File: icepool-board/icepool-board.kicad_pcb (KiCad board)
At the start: 4 copper layers, 90 x 40 mm, 101 parts, among them J1 PWR, J2 PWR_IN, J3 I2C, J4 SWD, J5 8P8C_Shielded, J6 8P8C_Shielded, SW1 B3U-1000P, U1 LD1117S33CTR, U2 LD1117S12CTR, U3 ATSAMD21E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

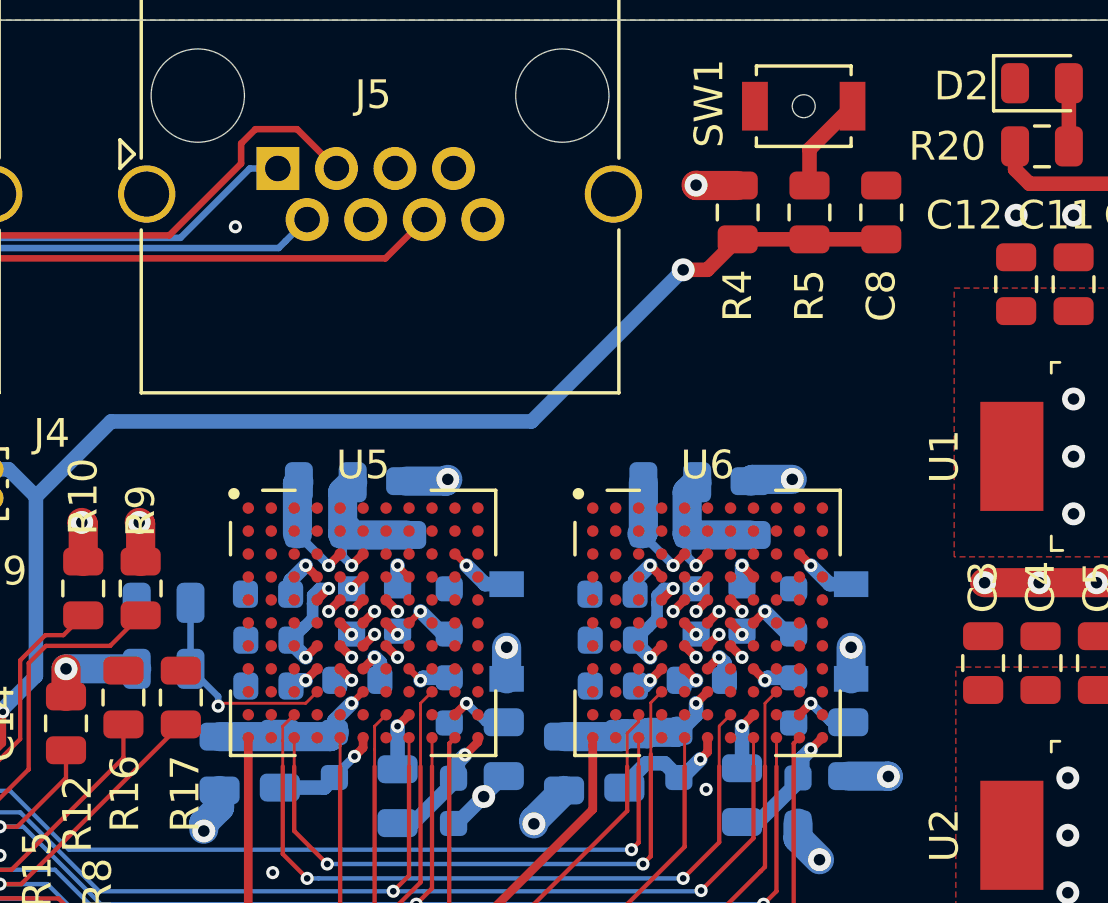
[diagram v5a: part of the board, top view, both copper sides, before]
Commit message: Fixed missing trace on FPGA0.
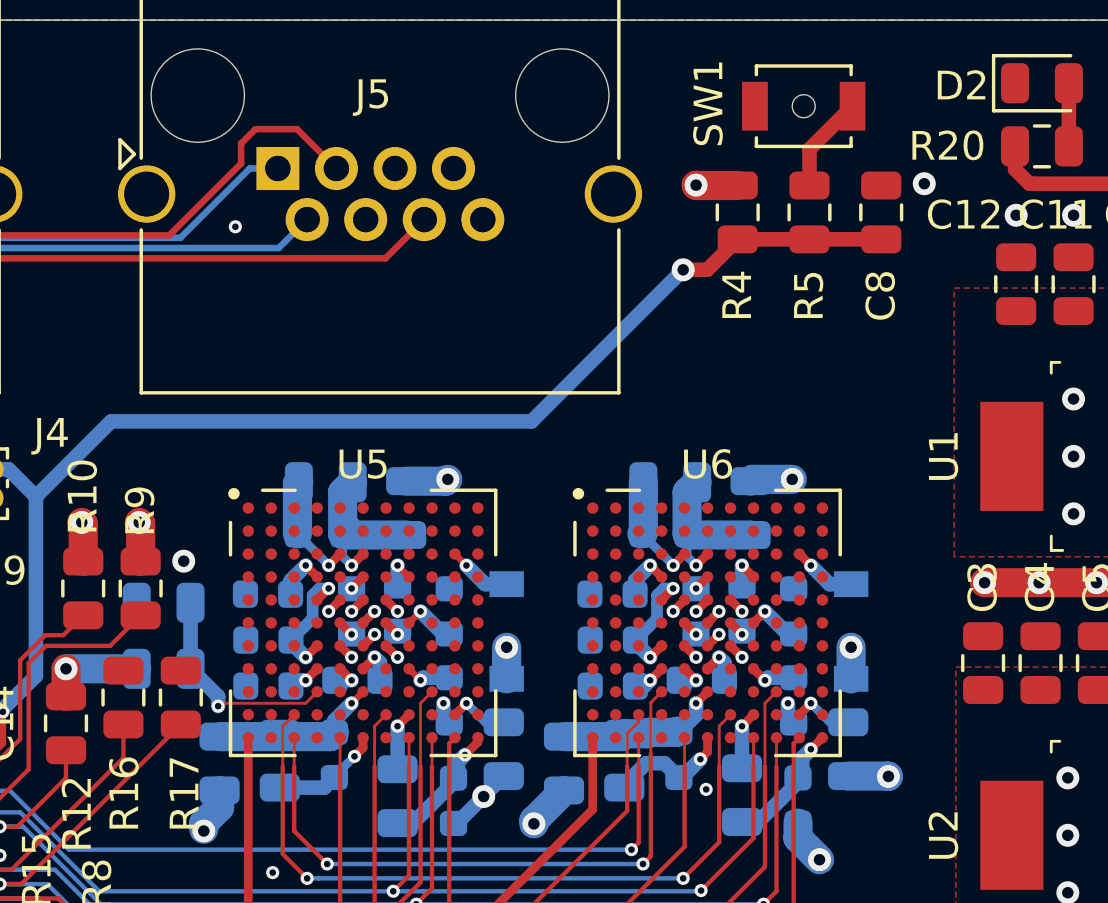
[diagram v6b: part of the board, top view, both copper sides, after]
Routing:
- net GND: track 49.8 -> 51.9 mm, vias 60 -> 64
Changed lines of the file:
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@@
     (thickness 1.6)
     (drawings 4)
-    (tracks 792)
+    (tracks 801)
     (zones 0)
     (modules 101)
@@
   (page A4)
   (layers
-    (0 F.Cu signal hide)
+    (0 F.Cu signal)
     (1 In1.Cu power hide)
     (2 In2.Cu power hide)
@@
     (32 B.Adhes user hide)
     (33 F.Adhes user hide)
-    (34 B.Paste user)
-    (35 F.Paste user)
-    (36 B.SilkS user)
-    (37 F.SilkS user)
-    (38 B.Mask user)
-    (39 F.Mask user)
+    (34 B.Paste user hide)
+    (35 F.Paste user hide)
+    (36 B.SilkS user hide)
+    (37 F.SilkS user hide)
+    (38 B.Mask user hide)
+    (39 F.Mask user hide)
     (40 Dwgs.User user hide)
     (41 Cmts.User user hide)
-    (42 Eco1.User user hide)
-    (43 Eco2.User user hide)
+    (42 Eco1.User user)
+    (43 Eco2.User user)
     (44 Edge.Cuts user)
     (45 Margin user hide)
-    (46 B.CrtYd user)
-    (47 F.CrtYd user)
-    (48 B.Fab user hide)
-    (49 F.Fab user hide)
+    (46 B.CrtYd user hide)
+    (47 F.CrtYd user hide)
+    (48 B.Fab user)
+    (49 F.Fab user)
   )
   (setup
@@
   (segment (start 89.8375 106.3375) (end 89.85 106.35) (width 1.016) (layer B.Cu) (net 1))
   (segment (start 88.45 106.3375) (end 89.8375 106.3375) (width 1.016) (layer B.Cu) (net 1))
+  (segment (start 70.5625 103) (end 71.15 103) (width 0.508) (layer B.Cu) (net 1))
+  (via (at 74.35 103.8) (size 0.4572) (drill 0.2286) (layers F.Cu B.Cu) (net 1))
+  (segment (start 74.35 104.2875) (end 74.55 104.4875) (width 0.508) (layer B.Cu) (net 1))
+  (segment (start 74.35 103.8) (end 74.35 104.2875) (width 0.508) (layer B.Cu) (net 1))
+  (via (at 86.35 103.8) (size 0.4572) (drill 0.2286) (layers F.Cu B.Cu) (net 1))
+  (segment (start 86.35 104.2875) (end 86.55 104.4875) (width 0.508) (layer B.Cu) (net 1))
+  (segment (start 86.35 103.8) (end 86.35 104.2875) (width 0.508) (layer B.Cu) (net 1))
+  (via (at 65.3 98.85) (size 0.8) (drill 0.4) (layers F.Cu B.Cu) (net 1))
+  (via (at 91.1 85.7) (size 0.8) (drill 0.4) (layers F.Cu B.Cu) (net 1))
   (segment (start 102.7 86.5) (end 102.7 86.5125) (width 0.508) (layer F.Cu) (net 2))
   (segment (start 104.381263 88.181263) (end 102.7 86.5) (width 0.508) (layer F.Cu) (net 2))
@@
   (segment (start 69.95 103.4) (end 69.55 103.8) (width 0.1016) (layer F.Cu) (net 242))
   (segment (start 69.55 103.8) (end 66.6 103.8) (width 0.1016) (layer F.Cu) (net 242))
-  (segment (start 66.5 103.5625) (end 65.5375 102.6) (width 0.2286) (layer B.Cu) (net 242))
-  (segment (start 66.5 103.9) (end 66.5 103.5625) (width 0.2286) (layer B.Cu) (net 242))
-  (segment (start 65.5375 102.6) (end 65.5375 100.3) (width 0.2286) (layer B.Cu) (net 242))
+  (segment (start 66.5 103.5625) (end 65.5375 102.6) (width 0.508) (layer B.Cu) (net 242))
+  (segment (start 66.5 103.9) (end 66.5 103.5625) (width 0.508) (layer B.Cu) (net 242))
+  (segment (start 65.5375 102.6) (end 65.5375 100.3) (width 0.508) (layer B.Cu) (net 242))
   (zone (net 5) (net_name +3V3) (layer F.Cu) (hatch edge 0.508)
     (priority 1)

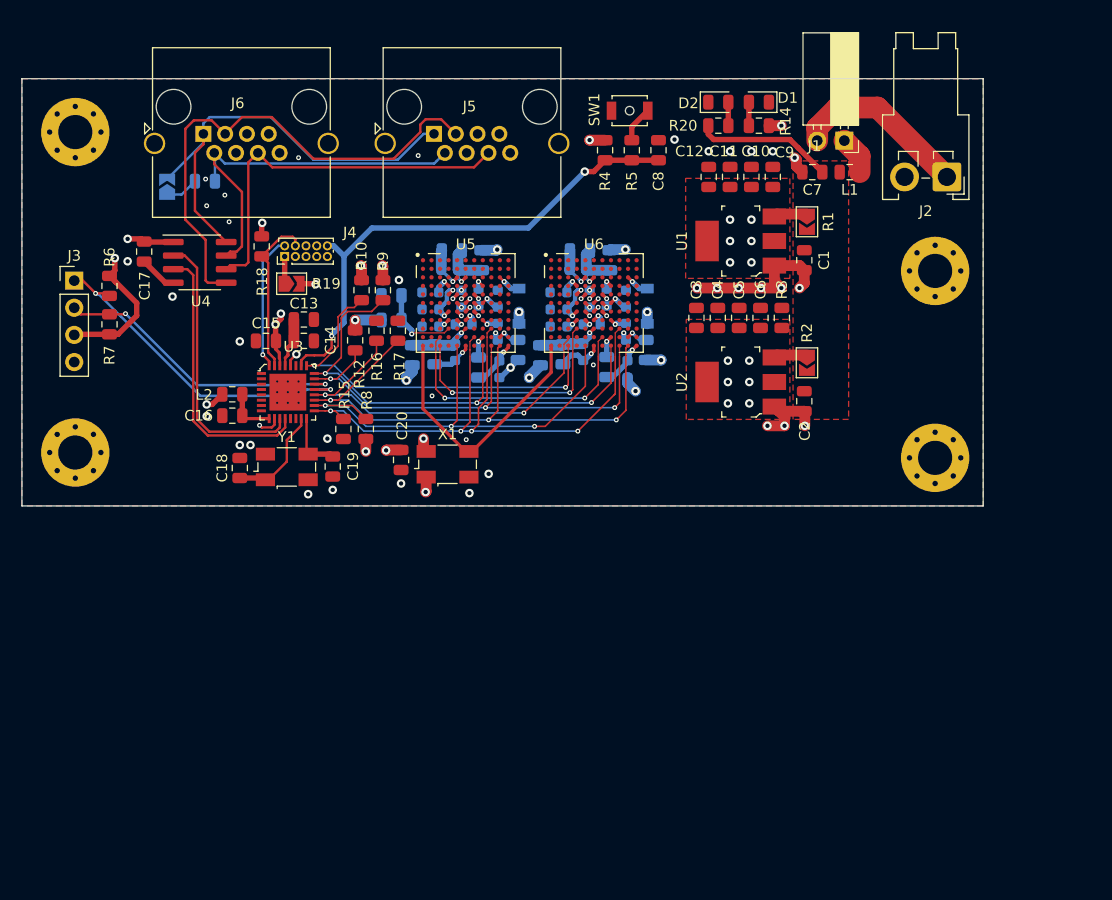
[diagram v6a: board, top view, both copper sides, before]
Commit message: Softened corners. Shrunk C29/C42 by 0.1mm for DRC.
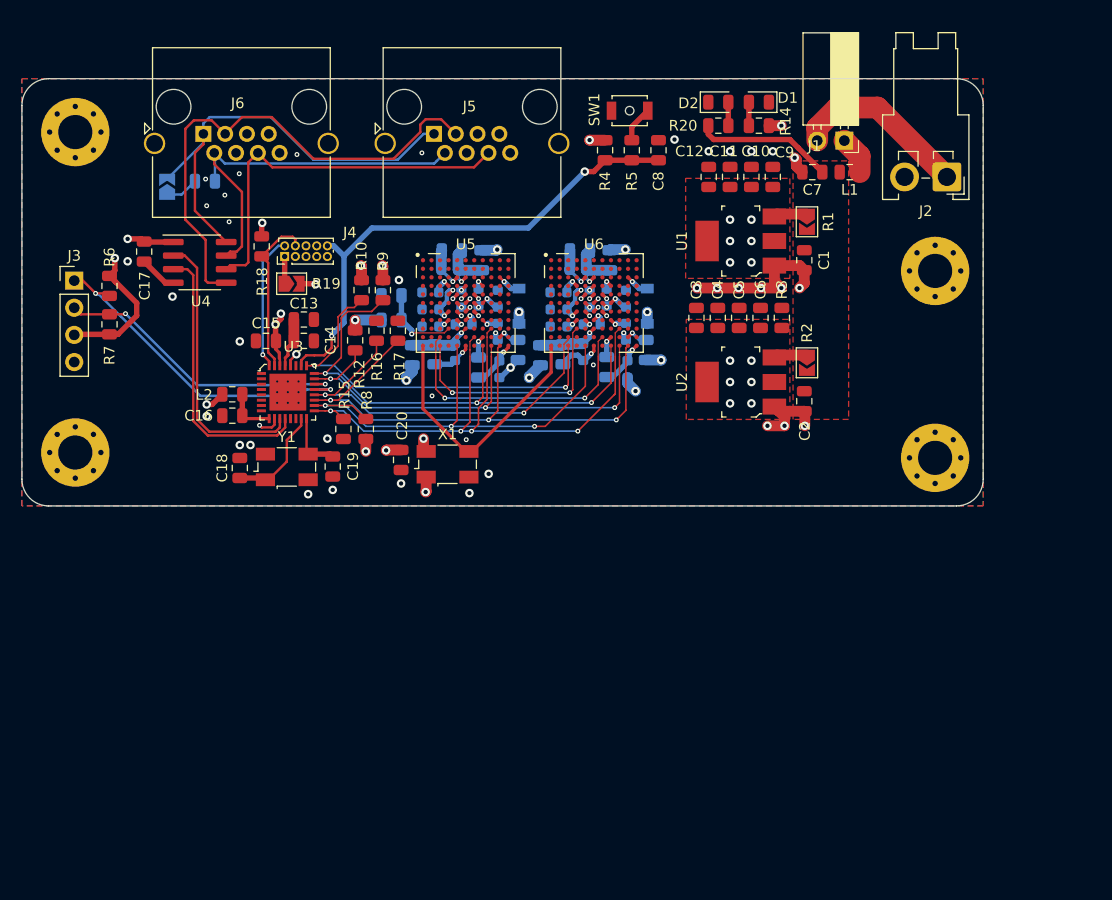
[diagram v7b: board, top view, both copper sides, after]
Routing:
- net GND: vias 64 -> 65
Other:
- outline, holes or cut-outs redrawn
- rule trace_min: 0.089 -> 0.0889

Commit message: Rethinking things...
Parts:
- J1: footprint Connector_PinSocket_2.54mm:PinSocket_1x02_P2.54mm_Horizontal -> Connector_PinSocket_2.54mm:PinSocket_1x02_P2.54mm_Vertical
- J2: footprint Connector_JST:JST_VH_S2P-VH_1x02_P3.96mm_Horizontal -> Connector_JST:JST_VH_B2P-VH_1x02_P3.96mm_Vertical
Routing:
- net +3V3: track 69.1 -> 71.5 mm
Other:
- board text added: "(c) fourside.io icepool-board v201910-0 github.com/jkiv/icepool-board"
